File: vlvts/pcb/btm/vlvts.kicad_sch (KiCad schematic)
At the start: 27 parts, among them J3 Conn_01x14_Female, M1 Motor_DC_ALT, U1 XC9110A, U2 XC9111C, U3 XC9111C, U4 DRV8210

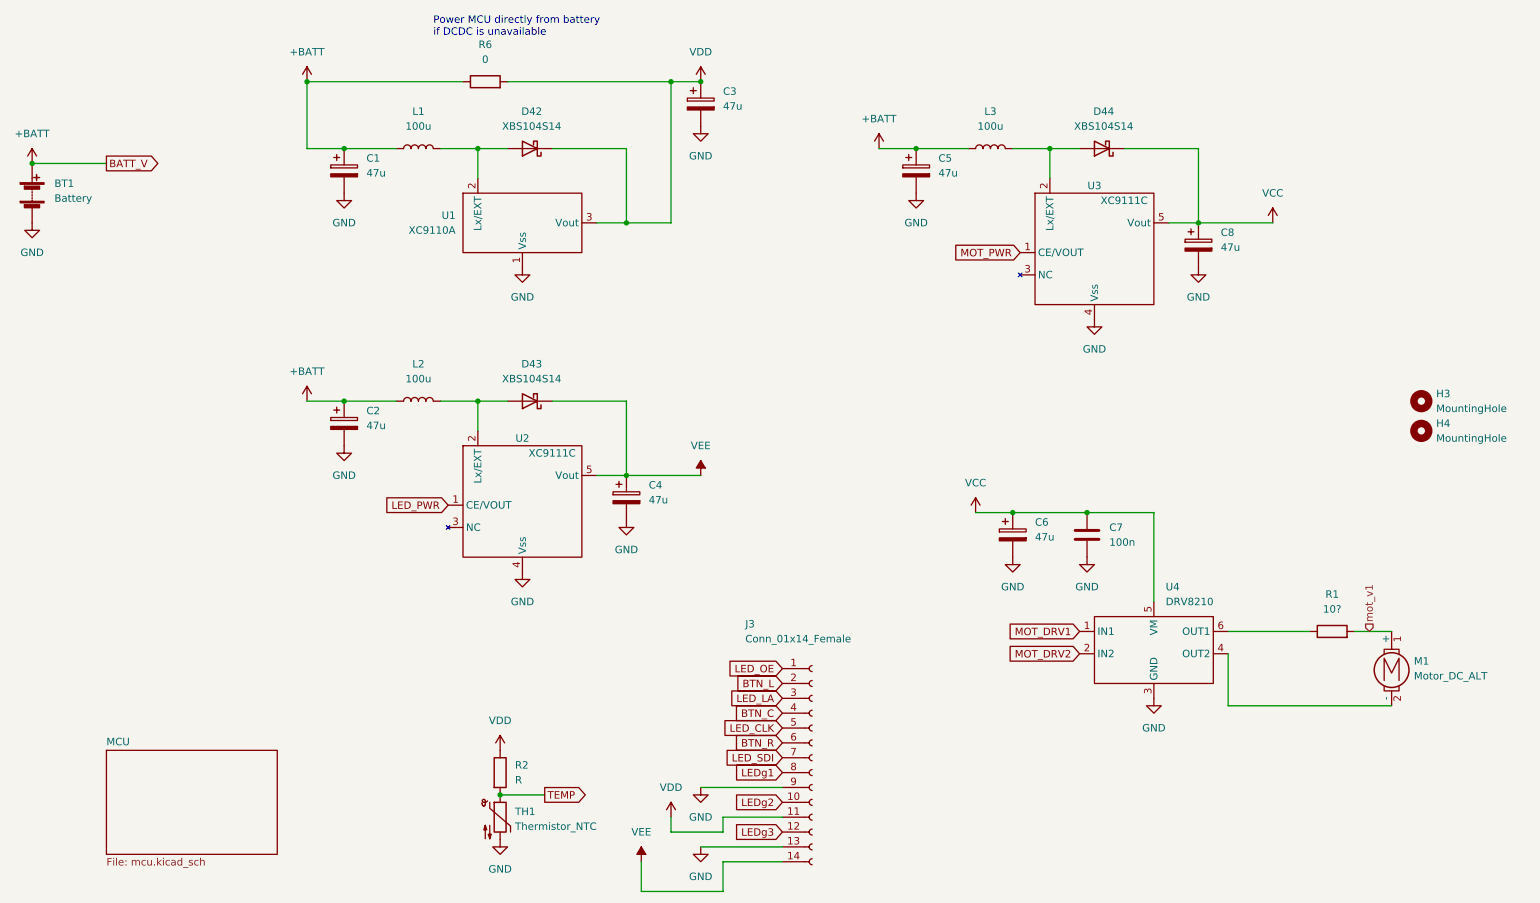
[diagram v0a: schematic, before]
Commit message: vlvts: partial updates to PCBs
Fixing problems spotted after the manufacturing of an initial batch
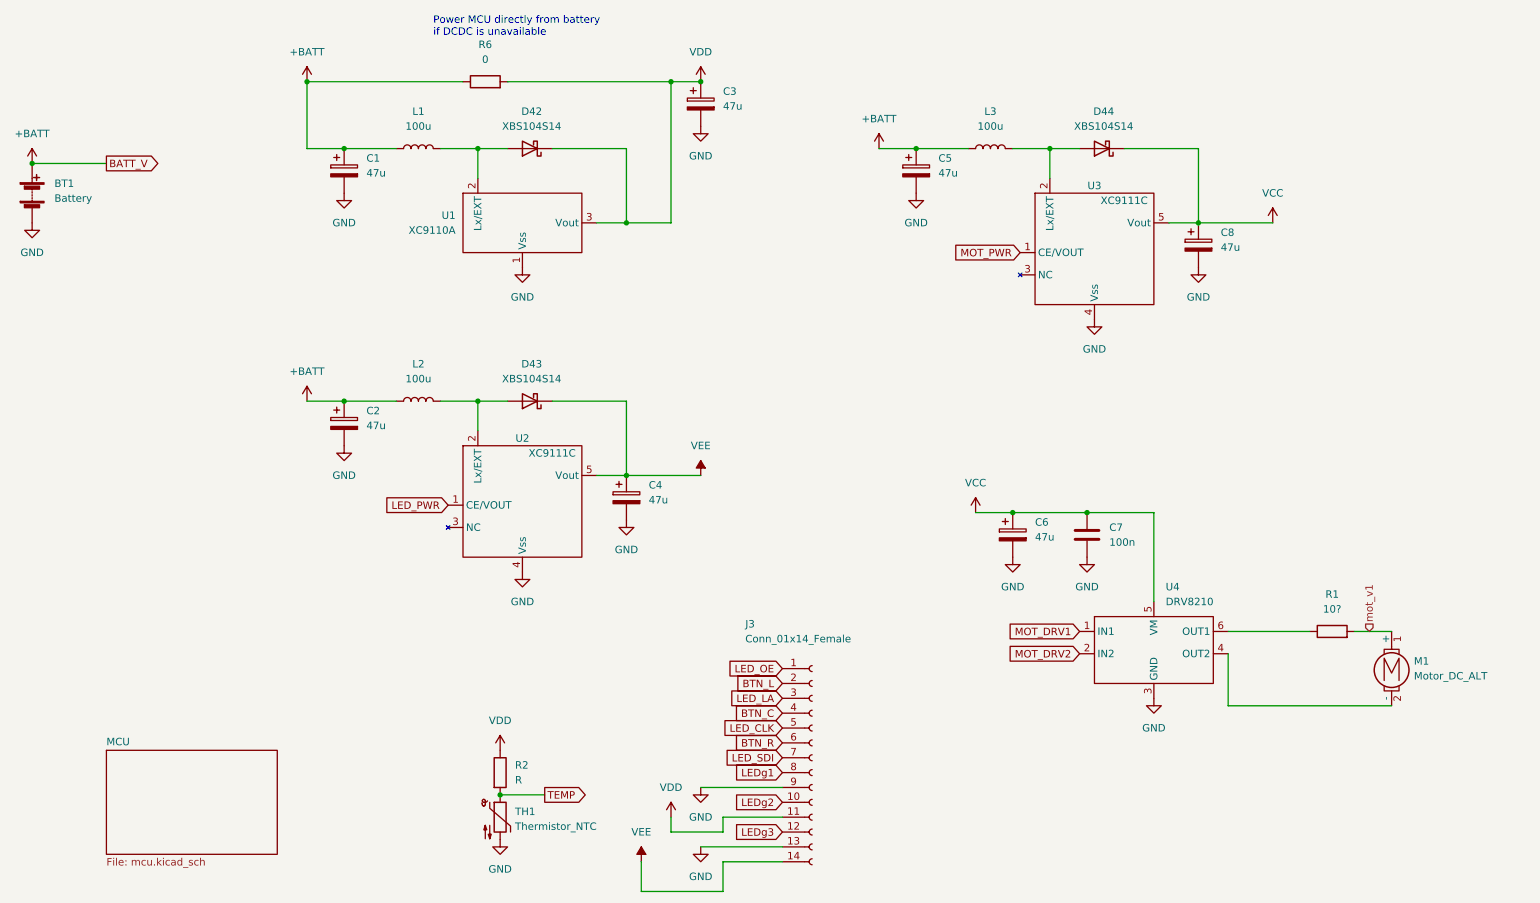
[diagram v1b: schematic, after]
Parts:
- removed H3, H4: MountingHole, MountingHole:MountingHole_2.5mm, symbol Mechanical:MountingHole
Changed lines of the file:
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@@
 (kicad_sch
-	(version 20231120)
+	(version 20250114)
 	(generator "eeschema")
-	(generator_version "8.0")
+	(generator_version "9.0")
 	(paper "A4")
+	(text "Power MCU directly from battery\nif DCDC is unavailable"
+		(exclude_from_sim no)
+		(at 96.52 17.78 0)
+		(effects
+			(font
+				(size 1.27 1.27)
+			)
+			(justify left bottom)
+		)
+	)
 	(junction
 		(at 201.93 36.83)
@@
 		)
 	)
-	(text "Power MCU directly from battery\nif DCDC is unavailable"
-		(exclude_from_sim no)
-		(at 96.52 17.78 0)
-		(effects
-			(font
-				(size 1.27 1.27)
-			)
-			(justify left bottom)
-		)
-	)
 	(global_label "LED_PWR"
 		(shape input)
@@
 		(shape input)
 		(at 256.54 119.38 90)
-		(fields_autoplaced yes)
 		(effects
 			(font
@@
 	)
 	(symbol
-		(lib_id "Mechanical:MountingHole")
-		(at 265.43 85.09 0)
-		(unit 1)
-		(exclude_from_sim no)
-		(in_bom yes)
-		(on_board yes)
-		(dnp no)
-		(fields_autoplaced yes)
-		(property "Reference" "H4"
-			(at 267.97 83.8199 0)
-			(effects
-				(font
-					(size 1.27 1.27)
-				)
-				(justify left)
-			)
-		)
-		(property "Value" "MountingHole"
-			(at 267.97 86.3599 0)
-			(effects
-				(font
-					(size 1.27 1.27)
-				)
-				(justify left)
-			)
-		)
-		(property "Footprint" "MountingHole:MountingHole_2.5mm"
-			(at 265.43 85.09 0)
-			(effects
-				(font
-					(size 1.27 1.27)
-				)
-				(hide yes)
-			)
-		)
-		(property "Datasheet" "~"
-			(at 265.43 85.09 0)
-			(effects
-				(font
-					(size 1.27 1.27)
-				)
-				(hide yes)
-			)
-		)
-		(property "Description" ""
-			(at 265.43 85.09 0)
-			(effects
-				(font
-					(size 1.27 1.27)
-				)
-				(hide yes)
-			)
-		)
-		(instances
-			(project ""
-				(path "/0c25e7b3-7d11-40fd-9acb-cfb2f5d15e7d"
-					(reference "H4")
-					(unit 1)
-				)
-			)
-		)
-	)
-	(symbol
 		(lib_id "power:GND")
 		(at 81.28 44.45 0)
@@
 	)
 	(symbol
-		(lib_id "Mechanical:MountingHole")
-		(at 265.43 80.01 0)
-		(unit 1)
-		(exclude_from_sim no)
-		(in_bom yes)
-		(on_board yes)
-		(dnp no)
-		(fields_autoplaced yes)
-		(property "Reference" "H3"
-			(at 267.97 78.7399 0)
-			(effects
-				(font
-					(size 1.27 1.27)
-				)
-				(justify left)
-			)
-		)
-		(property "Value" "MountingHole"
-			(at 267.97 81.2799 0)
-			(effects
-				(font
-					(size 1.27 1.27)
-				)
-				(justify left)
-			)
-		)
-		(property "Footprint" "MountingHole:MountingHole_2.5mm"
-			(at 265.43 80.01 0)
-			(effects
-				(font
-					(size 1.27 1.27)
-				)
-				(hide yes)
-			)
-		)
-		(property "Datasheet" "~"
-			(at 265.43 80.01 0)
-			(effects
-				(font
-					(size 1.27 1.27)
-				)
-				(hide yes)
-			)
-		)
-		(property "Description" ""
-			(at 265.43 80.01 0)
-			(effects
-				(font
-					(size 1.27 1.27)
-				)
-				(hide yes)
-			)
-		)
-		(instances
-			(project ""
-				(path "/0c25e7b3-7d11-40fd-9acb-cfb2f5d15e7d"
-					(reference "H3")
-					(unit 1)
-				)
-			)
-		)
-	)
-	(symbol
 		(lib_id "power:GND")
 		(at 129.54 100.33 0)
@@
 		(at 40.64 139.7)
 		(size 29.21 17.78)
+		(exclude_from_sim no)
+		(in_bom yes)
+		(on_board yes)
+		(dnp no)
 		(fields_autoplaced yes)
 		(stroke
@@
 		)
 	)
+	(embedded_fonts no)
 )

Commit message: vlvts: new pcb
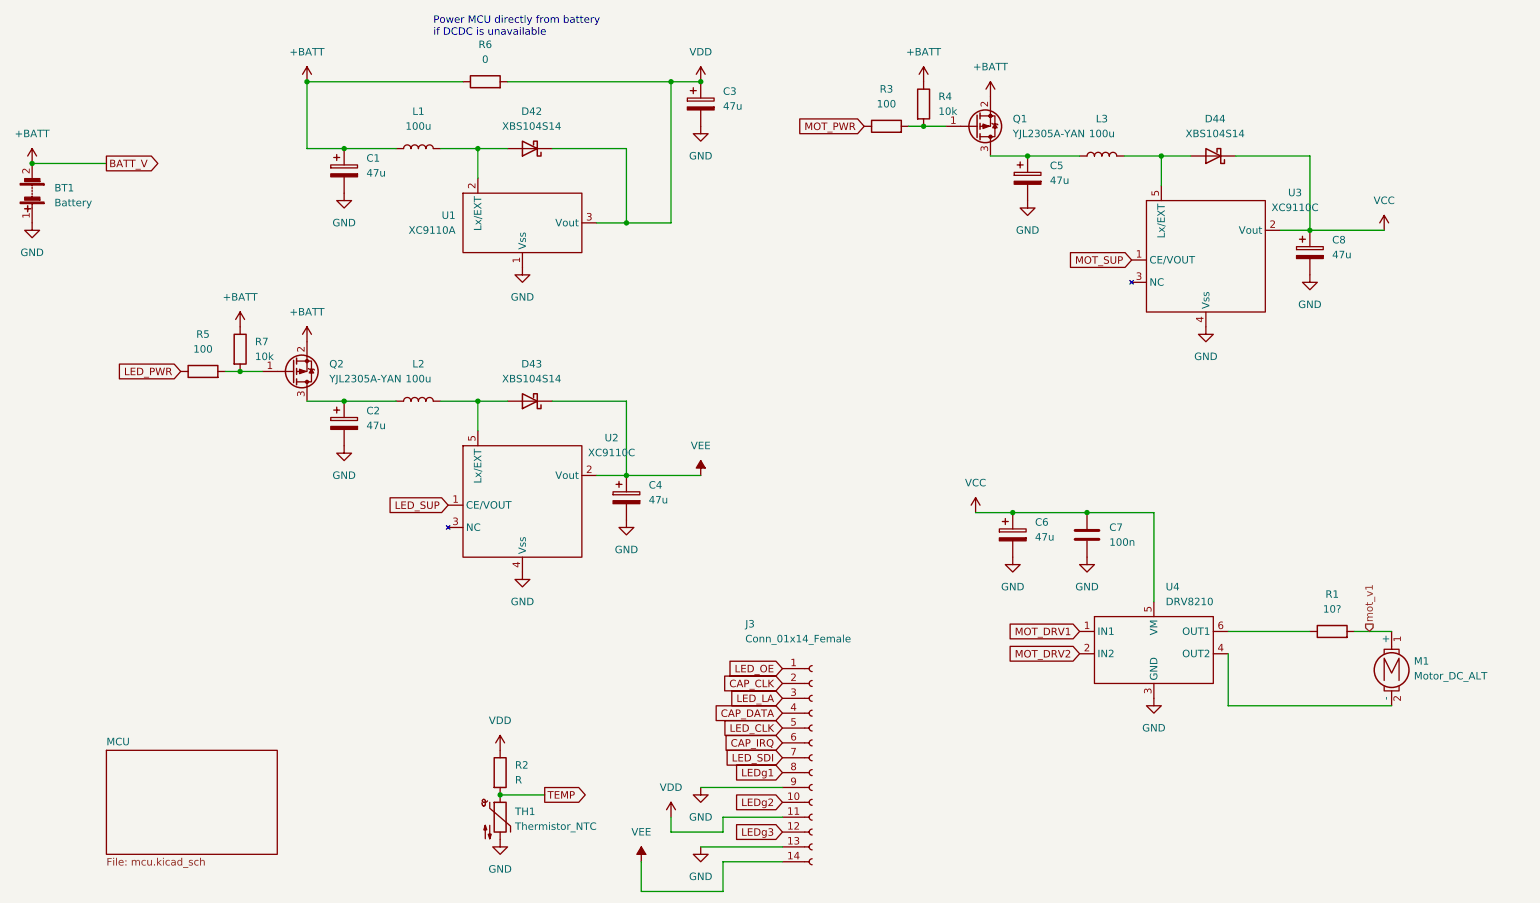
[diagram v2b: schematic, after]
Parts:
- removed U2, U3: XC9111C, Package_TO_SOT_SMD:SOT-23-5, symbol dcdc_torex:XC9111C
- added Q1, Q2: YJL2305A-YAN, Package_TO_SOT_SMD:SOT-23, symbol Transistor_FET:FDN340P
- added R3, R5: 100, Resistor_SMD:R_0603_1608Metric_Pad0.98x0.95mm_HandSolder, symbol Device:R
- added R4, R7: 10k, Resistor_SMD:R_0603_1608Metric_Pad0.98x0.95mm_HandSolder, symbol Device:R
- added U2, U3: XC9110C, Package_TO_SOT_SMD:SOT-23-5, symbol dcdc_torex:XC9110C
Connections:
- net +BATT: now also BT1.2 (-), Q1.2 (S), Q2.2 (S), R4.1, R7.1; no longer BT1.1 (+), C2.1, C5.1, L2.1, L3.1
- net GND: now also BT1.1 (+), U2.4 (Vss), U3.4 (Vss); no longer BT1.2 (-)
- net LED_PWR: now also R5.1
- net MOT_PWR: now also R3.1
- net VCC: now also U3.2 (Vout)
- net VEE: now also U2.2 (Vout)
- net at D44.2 (A), L3.2: now also U3.5 (Lx/EXT)
- net at D43.2 (A), L2.2: now also U2.5 (Lx/EXT)
- net BTN_C renamed CAP_DATA
- net BTN_L renamed CAP_CLK
- net BTN_R renamed CAP_IRQ
- new net: Q1.1 (G), R3.2, R4.2
- new net: C5.1, L3.1, Q1.3 (D)
- new net: C2.1, L2.1, Q2.3 (D)
- new net: Q2.1 (G), R5.2, R7.2
- new net LED_SUP: U2.1 (CE/VOUT)
- new net MOT_SUP: U3.1 (CE/VOUT)
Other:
- moved on the sheet: C5, C8, D44, L3
